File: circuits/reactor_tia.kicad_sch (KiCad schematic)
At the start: 18 parts, among them J1 Conn_01x04 OUT->AD7606, J2 Conn_01x02 +5V/GND, U1 OPA380AID, U2 OPA380AID

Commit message: refactor(circuits): redraw reactor TIA schematic with signal flow, power symbols, concise BOM
Rewrote gen_reactor_tia_sch.py to emit a hand-laid-out, left-to-right schematic (D1 -> U1 TIA with R_f||C_f feedback -> Sallen-Key U2 -> J1), real wires, +5V/GND power symbols, and net labels. Regenerated reactor_tia.kicad_sch. BOM Comment values trimmed to concise part values (full spec stays in Part Number/LCSC).
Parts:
- removed C1: 10pF C0G 50V, Capacitor_SMD:C_0603_1608Metric_Pad1.08x0.95mm_HandSolder, symbol viv:C
- removed C2: 2.2nF C0G 50V, Capacitor_SMD:C_0603_1608Metric_Pad1.08x0.95mm_HandSolder, symbol viv:C
- removed C3: 1nF C0G 50V, Capacitor_SMD:C_0603_1608Metric_Pad1.08x0.95mm_HandSolder, symbol viv:C
- removed C4: 10uF 25V X5R, Capacitor_SMD:C_0805_2012Metric_Pad1.18x1.45mm_HandSolder, symbol viv:C
- removed C5, C7: 100nF 50V X7R, Capacitor_SMD:C_0402_1005Metric_Pad0.74x0.62mm_HandSolder, symbol viv:C
- removed C6: 1uF 25V X7R, Capacitor_SMD:C_0402_1005Metric_Pad0.74x0.62mm_HandSolder, symbol viv:C
- removed R2, R3: 68k 1%, Resistor_SMD:R_0603_1608Metric_Pad0.98x0.95mm_HandSolder, symbol viv:R
- removed R4: 100k 1%, Resistor_SMD:R_0603_1608Metric_Pad0.98x0.95mm_HandSolder, symbol viv:R
- removed R5, R6: 10k 1%, Resistor_SMD:R_0603_1608Metric_Pad0.98x0.95mm_HandSolder, symbol viv:R
- removed U1, U2: OPA380AID, Package_SO:SOIC-8_3.9x4.9mm_P1.27mm, symbol viv:OPA380
- added C1: 10pF C0G, Capacitor_SMD:C_0603_1608Metric_Pad1.08x0.95mm_HandSolder, symbol viv:C_H
- added C2: 2.2nF C0G, Capacitor_SMD:C_0603_1608Metric_Pad1.08x0.95mm_HandSolder, symbol viv:C_V
- added C3: 1nF C0G, Capacitor_SMD:C_0603_1608Metric_Pad1.08x0.95mm_HandSolder, symbol viv:C_V
- added C4: 10uF, Capacitor_SMD:C_0805_2012Metric_Pad1.18x1.45mm_HandSolder, symbol viv:C_V
- added C5, C7: 100nF, Capacitor_SMD:C_0402_1005Metric_Pad0.74x0.62mm_HandSolder, symbol viv:C_V
- added C6: 1uF, Capacitor_SMD:C_0402_1005Metric_Pad0.74x0.62mm_HandSolder, symbol viv:C_V
- added R1: 10M, Resistor_SMD:R_0603_1608Metric_Pad0.98x0.95mm_HandSolder, symbol viv:R_H
- added R2, R3: 68k, Resistor_SMD:R_0603_1608Metric_Pad0.98x0.95mm_HandSolder, symbol viv:R_H
- added R4: 100k, Resistor_SMD:R_0603_1608Metric_Pad0.98x0.95mm_HandSolder, symbol viv:R_V
- added R5: 10k, Resistor_SMD:R_0603_1608Metric_Pad0.98x0.95mm_HandSolder, symbol viv:R_V
- added U1, U2: OPA380AID, Package_SO:SOIC-8_3.9x4.9mm_P1.27mm, symbol viv:OPA_N
- J1: value Conn_01x04 OUT->AD7606 -> Conn_01x04
- J2: value Conn_01x02 +5V/GND -> Conn_01x02
- R6: renamed from R1; value 10M 1% -> 10k; symbol viv:R -> viv:R_H; LCSC C57129 -> C25804; Part Number 0603WAF1005T5E -> 0603WAF1002T5E
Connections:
- net +5V: now also C5.1, C6.1, C7.1, R4.1, U1.7 (V+), U2.7 (V+)
- net GND: now also C3.2, C4.2, C5.2, C6.2, C7.2, R5.2, U1.4 (V-), U2.4 (V-)
- net VBIAS: now also R6.2, C4.1, U1.3 (+)
- net V_FILT: now also C2.1, U2.2 (-), U2.6
- net V_TIA: now also C1.2, R1.2, R2.1, U1.6; no longer R6.1
- net SUMMING: no longer names the net of D1.1 (K)
- net SUMMING: now also C1.1, R1.1, U1.2 (-); no longer R6.2
- new net: C2.2, R2.2, R3.1
- new net: C3.1, R3.2, U2.3 (+)
- new net: R4.2, R5.1, R6.1
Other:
- note added: "D1 / J1 / J2 = hand-add (THT)"
- note added: "Reactor TIA - bacteriorhodopsin M-state red read"
- note added: "TIA (size R_f for ~3 V red pedestal)"
- note added: "VBIAS divider (0.45 V)"
- note added: "anti-alias fc ~1.57 kHz"
- note added: "decoupling"
- note removed: "BIAS: zero-bias (D1 anode->GND). V_out RISES with light. 5V is plenty; 12V NOT needed."
- note removed: "D1 BPW34 (C85128) + J1/J2 = HAND-ADD (THT). JLCPCB SMT-places U1,U2,R*,C* only."
- note removed: "For 10 kHz BW only: lift D1 anode to a -5V ICL7660 charge pump (C_d ~20 pF)."
- note removed: "J1 -> AD7606: V_TIA=CHn (pedestal+signal), V_FILT=CHn+1 (anti-aliased)."
- note removed: "Reactor TIA - 2x OPA380AID (C201677) - red M-state read (JLCPCB)"
- note removed: "Sallen-Key 2-pole LP fc ~1.57 kHz (R2=R3=68k, C2=2.2n, C3=1n)."
- note removed: "U1=TIA U2=Sallen-Key anti-alias. OPA2380 dual is NOT stocked at JLCPCB -> 2 singles."
- note removed: "VBIAS = +5V * 10k/(100k+10k) = 0.45 V, RC-filtered (R6,C4). R_f sized so red pedestal ~3 V."
- title: Reactor TIA - 2x OPA380AID (JLCPCB) -> Reactor TIA - 2x OPA380AID
- moved on the sheet: R6

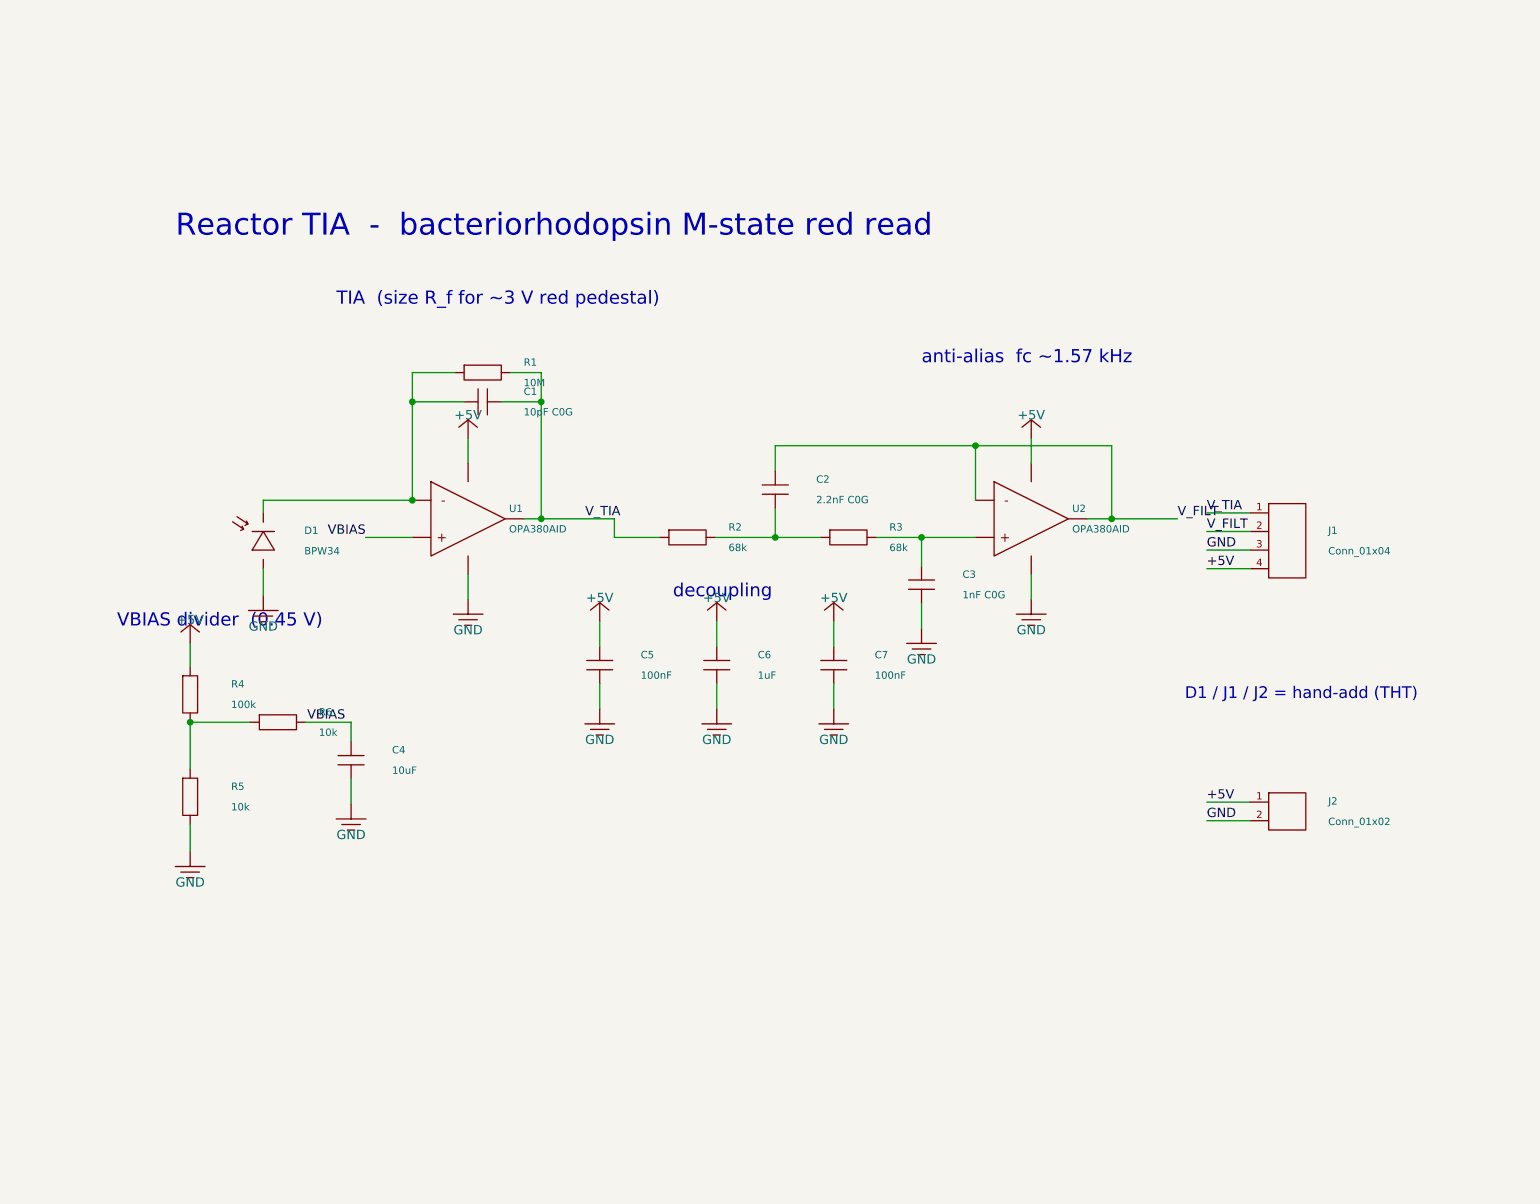
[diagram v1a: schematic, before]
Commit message: feat(circuits): dual-channel reactor TIA (1 OPA380 per channel)
Retire the single-channel 2-stage TIA (TIA + Sallen-Key). The board is now two independent channels, one OPA380AID TIA each (BPW34 -> TIA -> V_CHn), sharing one VBIAS divider. Anti-alias rides on the AD7606 oversampling instead of an analog filter stage; CH2 = matched ratiometric reference PD / 2nd plane.

Generator is the source of truth (parametric, N-channel). 14 SMT / 18 total, 8 nets, netlist-validated. README rewritten to per-channel topology + new BOM.
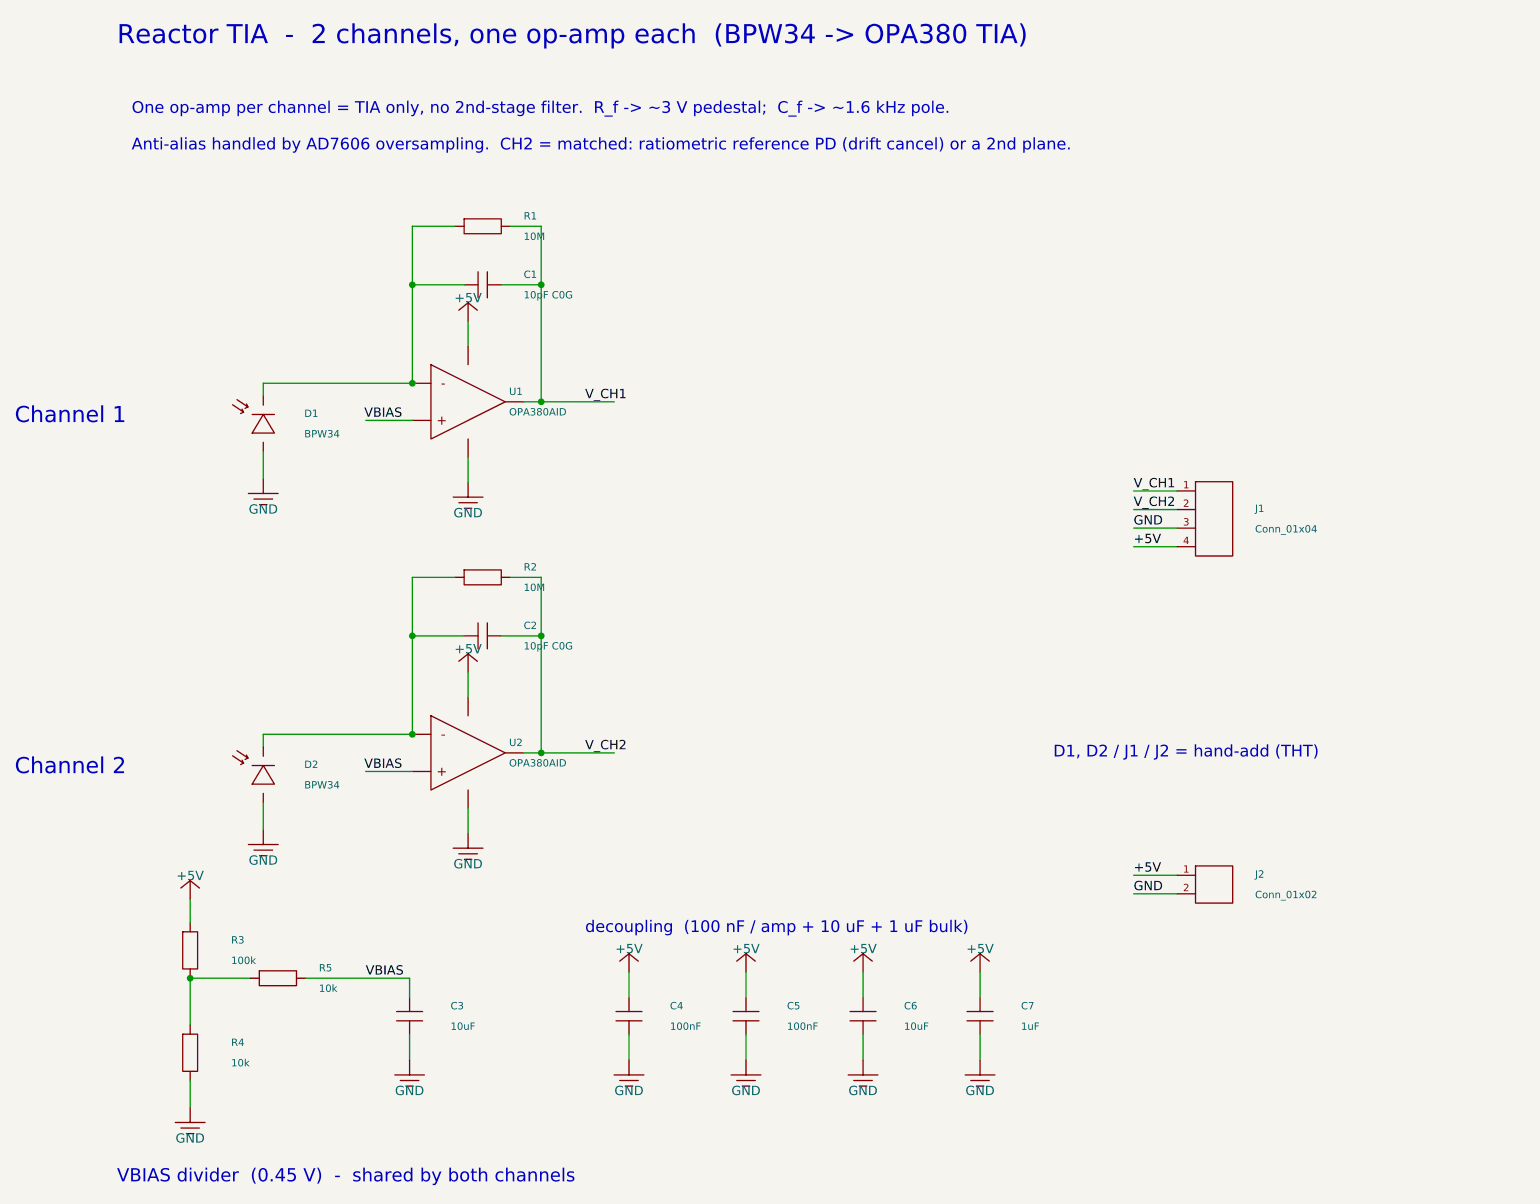
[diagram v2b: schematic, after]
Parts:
- removed C2: 2.2nF C0G, Capacitor_SMD:C_0603_1608Metric_Pad1.08x0.95mm_HandSolder, symbol viv:C_V
- removed R3: 68k, Resistor_SMD:R_0603_1608Metric_Pad0.98x0.95mm_HandSolder, symbol viv:R_H
- removed R5: 10k, Resistor_SMD:R_0603_1608Metric_Pad0.98x0.95mm_HandSolder, symbol viv:R_V
- removed R6: 10k, Resistor_SMD:R_0603_1608Metric_Pad0.98x0.95mm_HandSolder, symbol viv:R_H
- added C2: 10pF C0G, Capacitor_SMD:C_0603_1608Metric_Pad1.08x0.95mm_HandSolder, symbol viv:C_H
- added D2: BPW34, OptoDevice:Vishay_BPW34, symbol viv:PD
- added R3: 100k, Resistor_SMD:R_0603_1608Metric_Pad0.98x0.95mm_HandSolder, symbol viv:R_V
- added R5: 10k, Resistor_SMD:R_0603_1608Metric_Pad0.98x0.95mm_HandSolder, symbol viv:R_H
- C3: value 1nF C0G -> 10uF; footprint Capacitor_SMD:C_0603_1608Metric_Pad1.08x0.95mm_HandSolder -> Capacitor_SMD:C_0805_2012Metric_Pad1.18x1.45mm_HandSolder; LCSC C57112 -> C15850; Part Number CC0603JRNPO9BN102 -> CL21A106KAYNNNE
- C4: value 10uF -> 100nF; footprint Capacitor_SMD:C_0805_2012Metric_Pad1.18x1.45mm_HandSolder -> Capacitor_SMD:C_0402_1005Metric_Pad0.74x0.62mm_HandSolder; LCSC C15850 -> C1525; Part Number CL21A106KAYNNNE -> CL05B104KO5NNNC
- C6: value 1uF -> 10uF; footprint Capacitor_SMD:C_0402_1005Metric_Pad0.74x0.62mm_HandSolder -> Capacitor_SMD:C_0805_2012Metric_Pad1.18x1.45mm_HandSolder; LCSC C52923 -> C15850; Part Number CL05A105KA5NQNC -> CL21A106KAYNNNE
- C7: value 100nF -> 1uF; LCSC C1525 -> C52923; Part Number CL05B104KO5NNNC -> CL05A105KA5NQNC
- R2: value 68k -> 10M; LCSC C36871 -> C57129; Part Number 0603WAF6802T5E -> 0603WAF1005T5E
- R4: value 100k -> 10k; LCSC C25803 -> C25804; Part Number 0603WAF1003T5E -> 0603WAF1002T5E
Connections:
- net +5V: now also C4.1, R3.1; no longer R4.1
- net GND: now also R4.2, D2.2 (A)
- net VBIAS: now also C3.1, U2.3 (+), R5.2; no longer C4.1
- net V_CH2: now reaches R2.2
- net V_CH2: now also J1.2, U2.6, C2.2
- removed net V_FILT: J1.2, U2.2 (-), U2.6
- net V_TIA renamed V_CH1
- net V_CH1: no longer R2.1
- new net: C2.1, D2.1 (K), R2.1, U2.2 (-)
- new net: R3.2, R4.1, R5.1
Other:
- note added: "Anti-alias handled by AD7606 oversampling. CH2 = matched: ratiometric reference PD (drift cancel) or a 2nd plane."
- note added: "Channel 1"
- note added: "Channel 2"
- note added: "D1, D2 / J1 / J2 = hand-add (THT)"
- note added: "One op-amp per channel = TIA only, no 2nd-stage filter. R_f -> ~3 V pedestal; C_f -> ~1.6 kHz pole."
- note added: "Reactor TIA - 2 channels, one op-amp each (BPW34 -> OPA380 TIA)"
- note added: "VBIAS divider (0.45 V) - shared by both channels"
- note added: "decoupling (100 nF / amp + 10 uF + 1 uF bulk)"
- note removed: "D1 / J1 / J2 = hand-add (THT)"
- note removed: "Reactor TIA - bacteriorhodopsin M-state red read"
- note removed: "TIA (size R_f for ~3 V red pedestal)"
- note removed: "VBIAS divider (0.45 V)"
- note removed: "anti-alias fc ~1.57 kHz"
- note removed: "decoupling"
- title: Reactor TIA - 2x OPA380AID -> Reactor TIA - 2 channels x 1 OPA380AID
